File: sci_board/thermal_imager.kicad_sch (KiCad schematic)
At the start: 0 parts

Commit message: start SCI pcb
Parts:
- added J6: Conn_01x04_Pin, Connector_PinHeader_2.54mm:PinHeader_1x04_P2.54mm_Vertical, symbol Connector:Conn_01x04_Pin
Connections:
- net GND: now also J6.1 (Pin_1)
- net SCK: now also J6.2 (Pin_2)
- net SDA: now also J6.3 (Pin_3)
- net VIN: now also J6.4 (Pin_4)
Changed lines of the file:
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@@
 	(hierarchical_label "SCK"
 		(shape input)
-		(at 28.575 35.56 0)
+		(at 48.26 31.75 180)
 		(fields_autoplaced yes)
 		(effects
@@
 				(size 1.27 1.27)
 			)
-			(justify left)
+			(justify right)
 		)
 	)
 	(hierarchical_label "SDA"
 		(shape bidirectional)
-		(at 29.21 40.005 0)
+		(at 48.26 34.29 180)
 		(fields_autoplaced yes)
 		(effects
@@
 				(size 1.27 1.27)
 			)
-			(justify left)
+			(justify right)
 		)
 	)
 	(hierarchical_label "GND"
 		(shape input)
-		(at 28.575 31.75 0)
+		(at 48.26 29.21 180)
 		(fields_autoplaced yes)
 		(effects
@@
 				(size 1.27 1.27)
 			)
-			(justify left)
+			(justify right)
 		)
 	)
 	(hierarchical_label "VIN"
 		(shape input)
-		(at 29.21 27.94 0)
+		(at 48.26 36.83 180)
 		(fields_autoplaced yes)
 		(effects
@@
 				(size 1.27 1.27)
 			)
-			(justify left)
+			(justify right)
 		)
 	)
+	(symbol
+		(lib_id "Connector:Conn_01x04_Pin")
+		(at 53.34 31.75 0)
+		(mirror y)
+		(unit 1)
+		(exclude_from_sim no)
+		(in_bom yes)
+		(on_board yes)
+		(dnp no)
+		(fields_autoplaced yes)
+		(property "Reference" "J6"
+			(at 54.61 31.7499 0)
+			(effects
+				(font
+					(size 1.27 1.27)
+				)
+				(justify right)
+			)
+		)
+		(property "Value" "Conn_01x04_Pin"
+			(at 54.61 34.2899 0)
+			(effects
+				(font
+					(size 1.27 1.27)
+				)
+				(justify right)
+			)
+		)
+		(property "Footprint" "Connector_PinHeader_2.54mm:PinHeader_1x04_P2.54mm_Vertical"
+			(at 53.34 31.75 0)
+			(effects
+				(font
+					(size 1.27 1.27)
+				)
+				(hide yes)
+			)
+		)
+		(property "Datasheet" "~"
+			(at 53.34 31.75 0)
+			(effects
+				(font
+					(size 1.27 1.27)
+				)
+				(hide yes)
+			)
+		)
+		(property "Description" "Generic connector, single row, 01x04, script generated"
+			(at 53.34 31.75 0)
+			(effects
+				(font
+					(size 1.27 1.27)
+				)
+				(hide yes)
+			)
+		)
+		(pin "2"
+		)
+		(pin "1"
+		)
+		(pin "3"
+		)
+		(pin "4"
+		)
+		(instances
+			(project ""
+				(path "/b4b2c88d-f6cd-4e60-862d-e21f68728580/b65d9c5b-bcd6-4ca1-83d4-ac547dcb4ba6"
+					(reference "J6")
+					(unit 1)
+				)
+			)
+		)
+	)

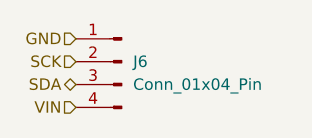
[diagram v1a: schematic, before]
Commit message: begin to update the pcb
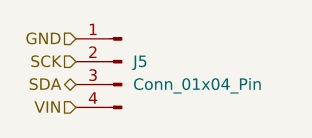
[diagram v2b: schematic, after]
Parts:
- renumbered J6 to J5
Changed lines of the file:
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@@
 		(dnp no)
 		(fields_autoplaced yes)
-		(property "Reference" "J6"
+		(property "Reference" "J5"
 			(at 54.61 31.7499 0)
 			(effects
@@
 			(project ""
 				(path "/b4b2c88d-f6cd-4e60-862d-e21f68728580/b65d9c5b-bcd6-4ca1-83d4-ac547dcb4ba6"
-					(reference "J6")
+					(reference "J5")
 					(unit 1)
 				)

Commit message: SCI BOM updated
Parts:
- J5: now not fitted
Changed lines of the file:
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@@
 		(in_bom yes)
 		(on_board yes)
-		(dnp no)
+		(dnp yes)
 		(fields_autoplaced yes)
 		(property "Reference" "J5"
@@
 			(at 53.34 31.75 0)
 			(effects
+				(font
+					(size 1.27 1.27)
+				)
+				(hide yes)
+			)
+		)
+		(property "Note" ""
+			(at 53.34 31.75 0)
+			(effects

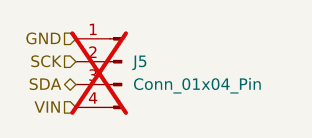
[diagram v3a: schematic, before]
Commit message: add decorations and labels to PCBs
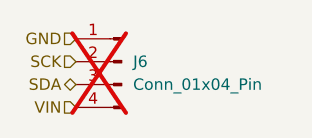
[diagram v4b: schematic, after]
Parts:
- renumbered J5 to J6
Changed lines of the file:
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@@
 		(dnp yes)
 		(fields_autoplaced yes)
-		(property "Reference" "J5"
+		(property "Reference" "J6"
 			(at 54.61 31.7499 0)
 			(effects
@@
 			(project ""
 				(path "/b4b2c88d-f6cd-4e60-862d-e21f68728580/b65d9c5b-bcd6-4ca1-83d4-ac547dcb4ba6"
-					(reference "J5")
+					(reference "J6")
 					(unit 1)
 				)

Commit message: use small connectors in corners and on sides for sun sensors and solar cells
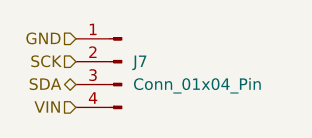
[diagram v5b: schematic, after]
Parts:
- J7: renamed from J6; Manufacturer (none) -> generic; Part Number (none) -> generic; now fitted
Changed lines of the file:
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@@
 		(in_bom yes)
 		(on_board yes)
-		(dnp yes)
+		(dnp no)
 		(fields_autoplaced yes)
-		(property "Reference" "J6"
+		(property "Reference" "J7"
 			(at 54.61 31.7499 0)
 			(effects
@@
 			)
 		)
+		(property "Manufacturer" "generic"
+			(at 53.34 31.75 0)
+			(effects
+				(font
+					(size 1.27 1.27)
+				)
+				(hide yes)
+			)
+		)
+		(property "Part Number" "generic"
+			(at 53.34 31.75 0)
+			(effects
+				(font
+					(size 1.27 1.27)
+				)
+				(hide yes)
+			)
+		)
+		(property "MANUFACTURER" ""
+			(at 53.34 31.75 0)
+			(effects
+				(font
+					(size 1.27 1.27)
+				)
+				(hide yes)
+			)
+		)
+		(property "MAXIMUM_PACKAGE_HEIGHT" ""
+			(at 53.34 31.75 0)
+			(effects
+				(font
+					(size 1.27 1.27)
+				)
+				(hide yes)
+			)
+		)
+		(property "PARTREV" ""
+			(at 53.34 31.75 0)
+			(effects
+				(font
+					(size 1.27 1.27)
+				)
+				(hide yes)
+			)
+		)
+		(property "STANDARD" ""
+			(at 53.34 31.75 0)
+			(effects
+				(font
+					(size 1.27 1.27)
+				)
+				(hide yes)
+			)
+		)
 		(pin "2"
 		)
@@
 			(project ""
 				(path "/b4b2c88d-f6cd-4e60-862d-e21f68728580/b65d9c5b-bcd6-4ca1-83d4-ac547dcb4ba6"
-					(reference "J6")
+					(reference "J7")
 					(unit 1)
 				)

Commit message: checking AUX and SCI, tweak BOM
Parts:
- J7: MANUFACTURER (none) -> generic; Manufacturer generic -> (none); PARTREV (none) -> 2.54mm pins 01x04; Part Number generic -> (none)
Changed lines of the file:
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@@
 			)
 		)
-		(property "Manufacturer" "generic"
-			(at 53.34 31.75 0)
-			(effects
-				(font
-					(size 1.27 1.27)
-				)
-				(hide yes)
-			)
-		)
-		(property "Part Number" "generic"
-			(at 53.34 31.75 0)
-			(effects
-				(font
-					(size 1.27 1.27)
-				)
-				(hide yes)
-			)
-		)
-		(property "MANUFACTURER" ""
+		(property "MANUFACTURER" "generic"
 			(at 53.34 31.75 0)
 			(effects
@@
 			)
 		)
-		(property "PARTREV" ""
+		(property "PARTREV" "2.54mm pins 01x04"
 			(at 53.34 31.75 0)
 			(effects

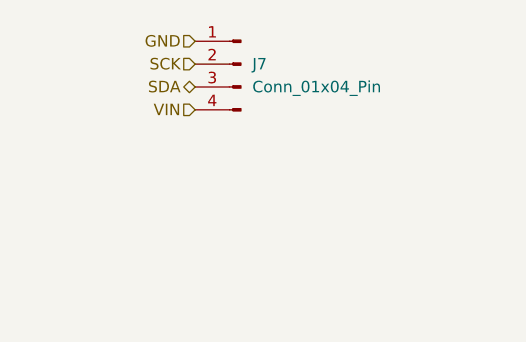
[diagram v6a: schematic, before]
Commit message: full science board with camera switches
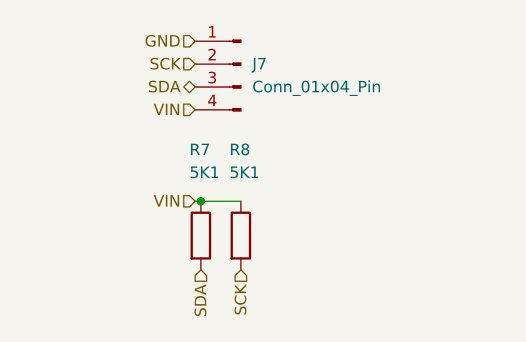
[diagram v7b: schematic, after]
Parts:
- added R7, R8: 5K1, Resistor_SMD:R_0402_1005Metric_Pad0.72x0.64mm_HandSolder, symbol Device:R
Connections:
- net SCK: now also R8.2
- net SDA: now also R7.2
- net VIN: now also R7.1, R8.1

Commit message: cleanup and bom
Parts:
- J7: value Conn_01x04_Pin -> Conn_01x04_Pin Vertical
- renumbered R7 to R25, R8 to R26
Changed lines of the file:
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@@
 		(on_board yes)
 		(dnp no)
-		(property "Reference" "R7"
+		(property "Reference" "R25"
 			(at 47.625 41.275 0)
 			(effects
@@
 			(project "sci_board"
 				(path "/b4b2c88d-f6cd-4e60-862d-e21f68728580/b65d9c5b-bcd6-4ca1-83d4-ac547dcb4ba6"
-					(reference "R7")
+					(reference "R25")
 					(unit 1)
 				)
@@
 		(on_board yes)
 		(dnp no)
-		(property "Reference" "R8"
+		(property "Reference" "R26"
 			(at 52.07 41.275 0)
 			(effects
@@
 			(project "sci_board"
 				(path "/b4b2c88d-f6cd-4e60-862d-e21f68728580/b65d9c5b-bcd6-4ca1-83d4-ac547dcb4ba6"
-					(reference "R8")
+					(reference "R26")
 					(unit 1)
 				)
@@
 			)
 		)
-		(property "Value" "Conn_01x04_Pin"
+		(property "Value" "Conn_01x04_Pin Vertical"
 			(at 54.61 34.2899 0)
 			(effects
